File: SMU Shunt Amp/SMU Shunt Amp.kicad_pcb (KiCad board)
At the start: 2 copper layers, 99.1 x 54.6 mm, 45 parts, among them J1 30VDC, J2 Input, J3 Output, U1 LT3088, U2 TLE2426xD, U3 OPA189IDBVx, U4 THS4021CxDGNx

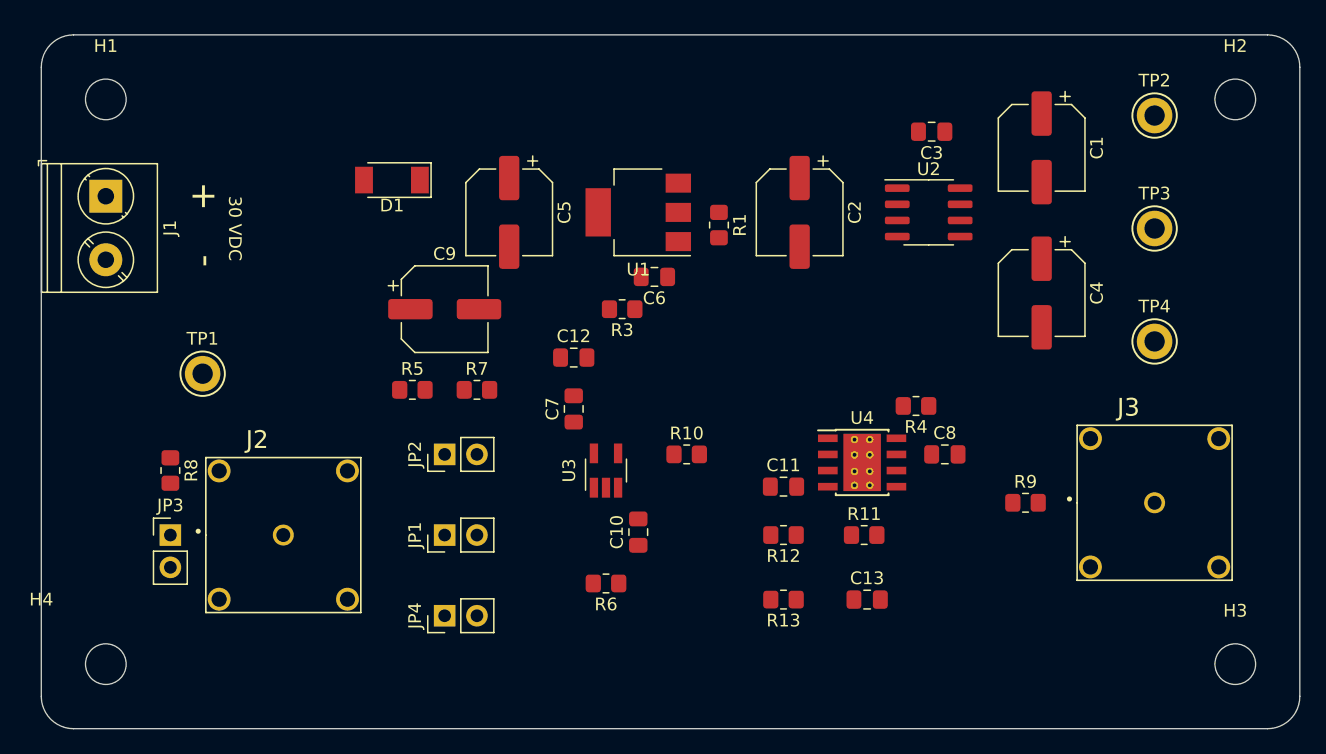
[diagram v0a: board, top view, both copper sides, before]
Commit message: Fix null pin and add thermal pad pin to THS 4021
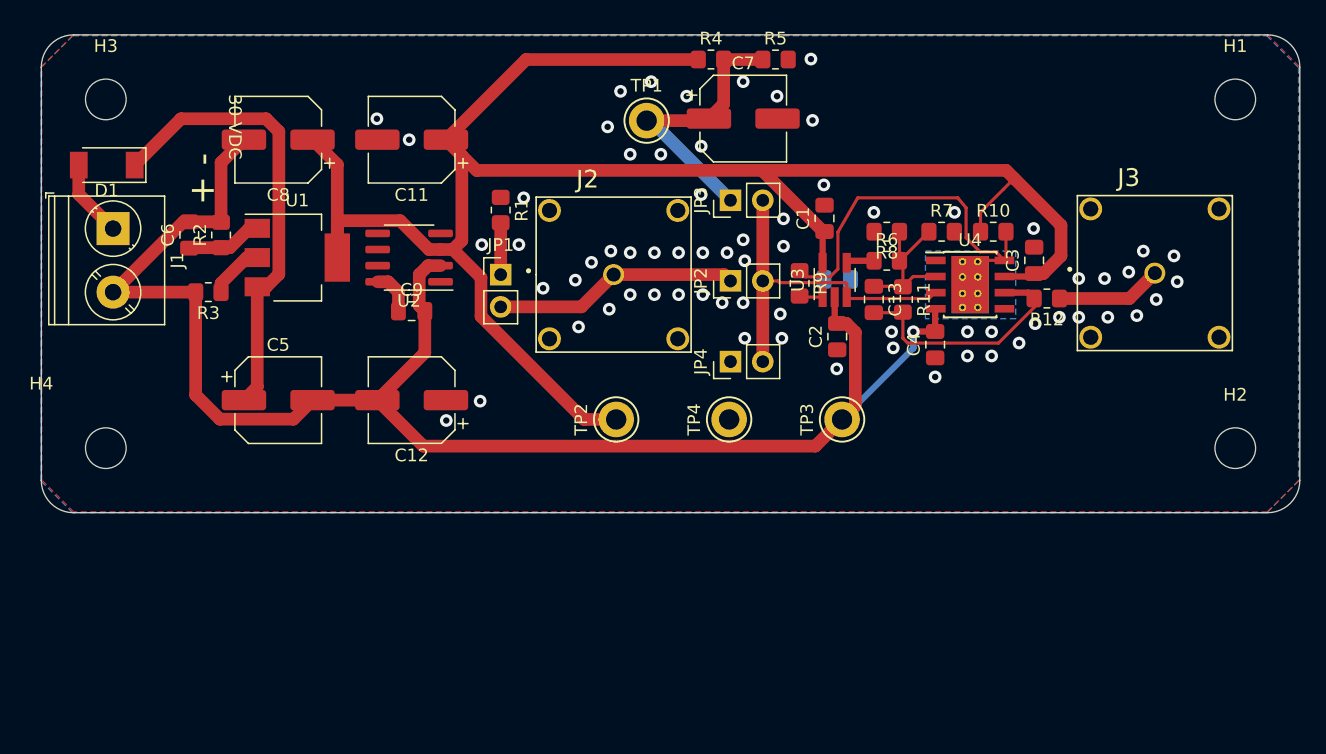
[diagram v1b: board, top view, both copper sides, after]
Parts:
- C10: renamed from C12; moved to B.Cu
- moved C12 50.3 mm to (99.0, 60.5), turned to 180 degrees
- moved C11 49.6 mm to (99.0, 40.0), turned to 180 degrees
- moved TP2 48.7 mm to (115.1, 62.0), turned to 90 degrees
- moved C9 43.3 mm to (99.0, 53.5), turned to 0 degrees
- moved C8 41.4 mm to (88.5, 40.0), turned to 180 degrees
- moved U2 41.1 mm to (98.8, 49.3), turned to 180 degrees
- moved R3 40.5 mm to (83.0, 52.0), turned to 180 degrees
- moved TP1 40.2 mm to (117.5, 38.5)
- moved C6 36.8 mm to (81.5, 47.5), turned to 90 degrees
- moved TP4 36.7 mm to (124.0, 62.0), turned to 90 degrees
- moved R4 35.0 mm to (122.6, 33.7)
- moved R5 35.0 mm to (127.6, 33.7)
- moved J2 33.1 mm to (114.9, 50.6)
- moved JP1 33.1 mm to (106.0, 50.6)
- moved R1 33.1 mm to (106.0, 45.5)
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- renumbered C7 to C1, C1 to C11, C4 to C12, C10 to C2, C8 to C3, C11 to C4, C9 to C7, C2 to C8, C3 to C9, H2 to H1, H3 to H2, H1 to H3, JP3 to JP1, JP1 to JP2, JP2 to JP3, R8 to R1, R4 to R10, R9 to R12, R3 to R2, R1 to R3, R5 to R4, R7 to R5, R10 to R6, R12 to R7, R13 to R8, R6 to R9, TP4 to TP3, TP3 to TP4
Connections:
- net NULL renamed NULLA
- U4 pad 9: (no net) -> Net-(U4-Pad9)
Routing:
- net +15V: track 0.00 -> 152.9 mm
- net -15V: track 0.00 -> 124.8 mm, vias 0 -> 1
- net Net-(C5-Pad1): track 0.00 -> 36.0 mm
- net NULLA: track 0.00 -> 28.1 mm
- net Net-(JP2-Pad2): track 0.00 -> 27.6 mm
- net Net-(C7-Pad1): track 0.00 -> 22.4 mm
- net Net-(J2-Pad1): track 0.00 -> 19.3 mm
- net Net-(C13-Pad2): track 0.00 -> 19.2 mm
- net Net-(C13-Pad1): track 0.00 -> 12.9 mm
- net Net-(J3-Pad1): track 0.00 -> 8.33 mm
- net Net-(D1-Pad2): track 0.00 -> 6.12 mm
- net Net-(C6-Pad1): track 0.00 -> 6.00 mm
- net Net-(JP1-Pad1): track 0.00 -> 4.08 mm
- net Net-(C9-Pad1): track 0.00 -> 3.48 mm
- net Net-(C10-Pad2): track 0.00 -> 2.21 mm
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- added copper zone on B.Cu, net GND
- added copper zone on F.Cu, net GND
- added copper zone on In1.Cu, net GND
- added copper zone on In2.Cu, net GND
- added copper zone on B.Cu, net Net-(U4-Pad9)
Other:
- board size 99.1 x 54.6 mm -> 99.1 x 37.6 mm
- copper layers 2 -> 4

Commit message: PCB sent to manufacturer.
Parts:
- removed the C11 at (99.0, 40.0)
- removed the C12 at (99.0, 60.5)
- removed the C8 at (88.5, 40.0)
- added C10: 10u, Capacitor_SMD:CP_Elec_6.3x7.7, F.Cu at (88.5, 40.0)
- added C14: 10u, Capacitor_SMD:CP_Elec_6.3x7.7, F.Cu at (98.9, 40.0)
- added C15: 10u, Capacitor_SMD:CP_Elec_6.3x7.7, F.Cu at (99.0, 60.5)
- added C5: 100n, Capacitor_SMD:C_0805_2012Metric_Pad1.18x1.45mm_HandSolder, B.Cu at (136.9, 49.8)
- added C6: 100n, Capacitor_SMD:C_0805_2012Metric_Pad1.18x1.45mm_HandSolder, B.Cu at (144.9, 58.2)
- added R13: 0R, Resistor_SMD:R_0805_2012Metric_Pad1.20x1.40mm_HandSolder, B.Cu at (136.9, 52.1)
- added R9: 0R, Resistor_SMD:R_0805_2012Metric_Pad1.20x1.40mm_HandSolder, B.Cu at (144.8, 55.2)
- added U5: OPA1611AIDR, Package_SO:SOIC-8_3.9x4.9mm_P1.27mm, B.Cu at (142.9, 51.4)
- JP1: value Jumper -> Term
- JP2: value Signal Input -> SIG
- JP3: value 100uV Input -> 100uV
- JP4: value Short to Ground -> GND
- R12: renamed from R11; value 147R -> 1.47K
- R7: value 147R -> 1.47K
- TP1: value TestPoint -> 100uV
- TP2: value TestPoint -> +14V
- TP3: value TestPoint -> -14V
- TP4: value TestPoint -> GND
- moved JP2 2.39 mm to (126.2, 52.2), turned to 180 degrees
- moved JP1 0.89 mm to (105.1, 50.6)
- moved R1 0.85 mm to (105.2, 45.5)
- renumbered C9 to C11, C10 to C12, C5 to C7, C7 to C8, C6 to C9, R9 to R10, R10 to R11, R12 to R14, R4 to R2, R5 to R3, R2 to R4, R3 to R5, U3 to U2, U4 to U3, U2 to U4
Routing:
- net -15V: track 124.8 -> 84.9 mm, vias 1 -> 3
- net Net-(C12-Pad1): track 1.84 -> 16.9 mm
- net GND: track 0.11 -> 5.51 mm, vias 68 -> 37
- net Net-(R9-Pad1): track 0.00 -> 4.64 mm
- net Net-(C13-Pad2): track 19.2 -> 22.7 mm, vias 0 -> 1
- net Net-(J2-Pad1): track 19.3 -> 22.8 mm
- net Net-(R13-Pad1): track 0.00 -> 2.51 mm
- net +15V: track 152.9 -> 155.1 mm, vias 0 -> 5
- net Net-(C8-Pad1): track 22.4 -> 20.3 mm
- net Net-(JP2-Pad2): track 27.6 -> 29.6 mm
- net Net-(C12-Pad2): track 2.21 -> 3.92 mm, vias 0 -> 1
- net NULLA: track 28.1 -> 26.8 mm
- added copper zone on In1.Cu, net (none)
- added copper zone on In2.Cu, net (none)
- added copper zone on F.Cu, net -15V
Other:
- board text added: "-V"
- board text added: ">"
- board text added: "Current Shunt Amp Prototype"
- board text added: "MAGI 2021"
- board text added: "SN:"
- board text removed: "+"
- board text removed: "-"

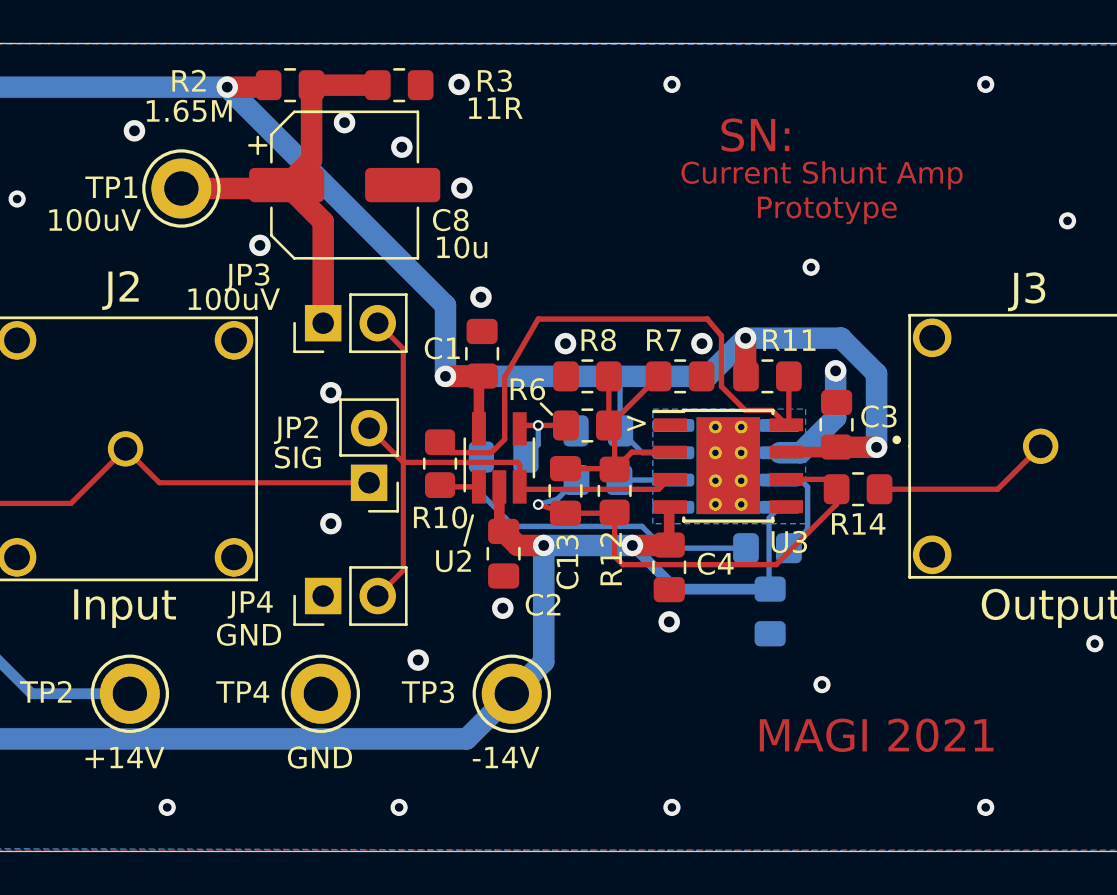
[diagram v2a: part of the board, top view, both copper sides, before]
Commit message: Rev B changes. THS4021 footprint fix, nulling circuit corrections, gnd tp cur limit.
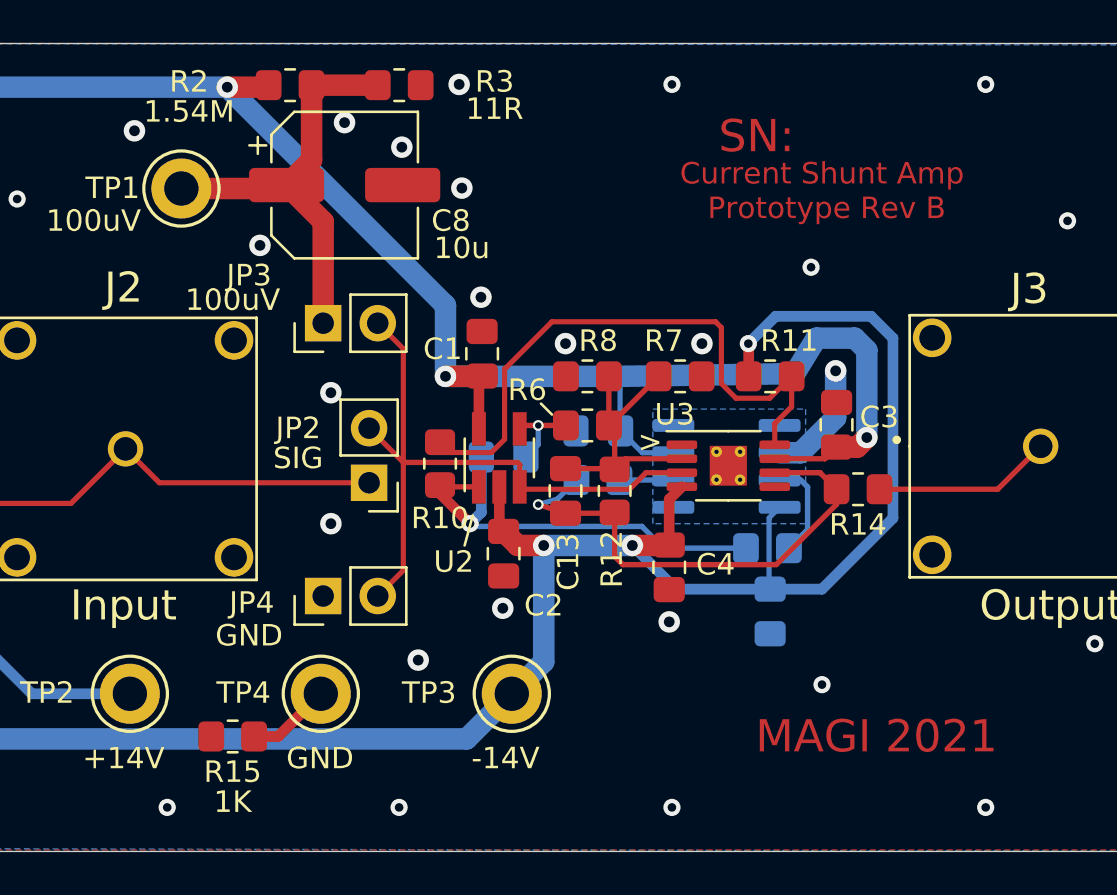
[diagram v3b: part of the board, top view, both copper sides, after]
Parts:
- added R15: 1K, Resistor_SMD:R_0805_2012Metric_Pad1.20x1.40mm_HandSolder, F.Cu at (119.9, 64.0)
- R11: value 20K -> 56K
- R2: value 1.65M -> 1.54M
- U3: footprint Package_SO:TI_SO-PowerPAD-8_ThermalVias -> Package_SO:MSOP-8-1EP_3x3mm_P0.65mm_EP1.73x1.85mm_ThermalVias
- moved R11 0.13 mm to (144.9, 47.2), turned to 180 degrees
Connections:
- R11 pad 1: +15V -> NULLA
- R11 pad 2: NULLA -> -15V
- TP4 pad 1: GND -> Net-(R15-Pad1)
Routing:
- net -15V: track 84.9 -> 110.8 mm, vias 3 -> 4
- net Net-(C12-Pad1): track 16.9 -> 22.6 mm, vias 0 -> 1
- net Net-(R15-Pad1): track 0.00 -> 3.93 mm
- net Net-(C13-Pad2): track 22.7 -> 24.1 mm
- net NULLA: track 26.8 -> 27.9 mm
- net +15V: track 155.1 -> 154.1 mm, vias 5 -> 4
- net Net-(JP2-Pad2): track 29.6 -> 30.3 mm
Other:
- board text added: "Current Shunt Amp Prototype Rev B"
- board text removed: "Current Shunt Amp Prototype"
